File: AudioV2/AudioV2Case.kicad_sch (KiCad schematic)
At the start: 0 parts

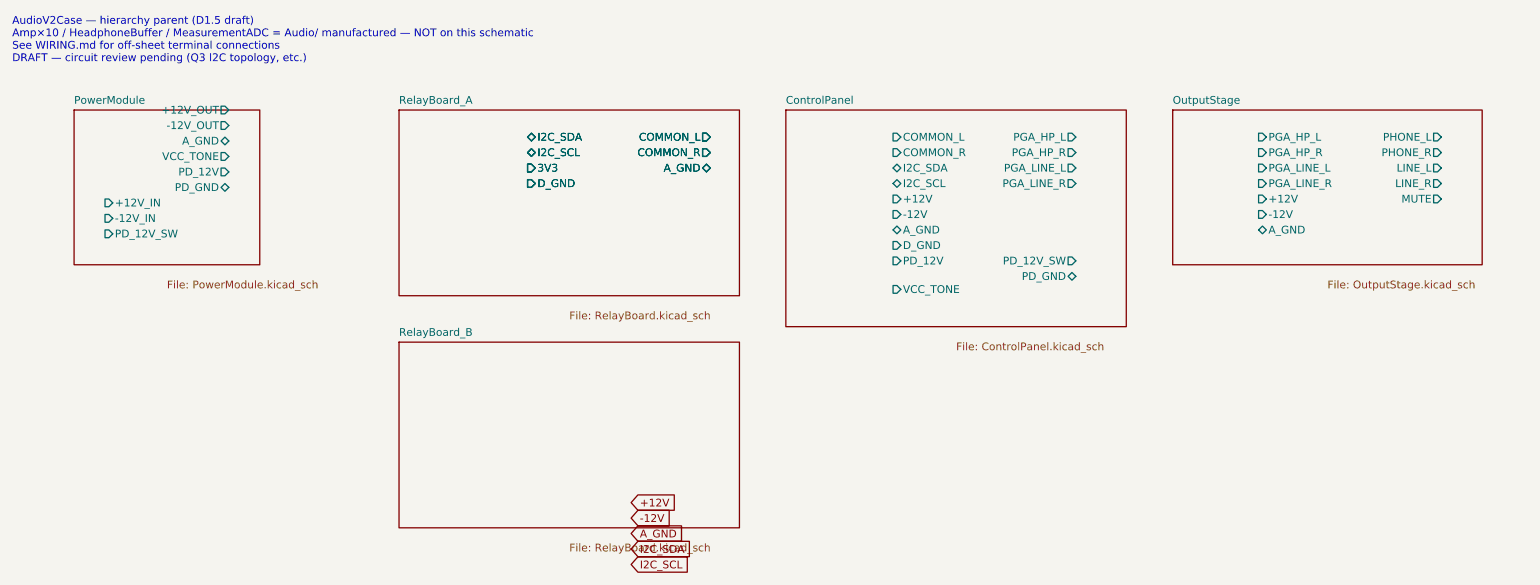
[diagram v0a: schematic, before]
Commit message: feat(AudioV2): CIRCUIT_DESIGNに沿って回路配置・配線（Control/Power/親）
- wire_circuit_design.py: PT2314 周辺 C/R、PGA2310 SPI/電源、7809、親バス
- PowerModule/ControlPanel/AudioV2Case を配線付きで再生成
- CIRCUIT_DESIGN.md チェックリスト更新

ERC は Relay/Output 未配線・親バス調整残り
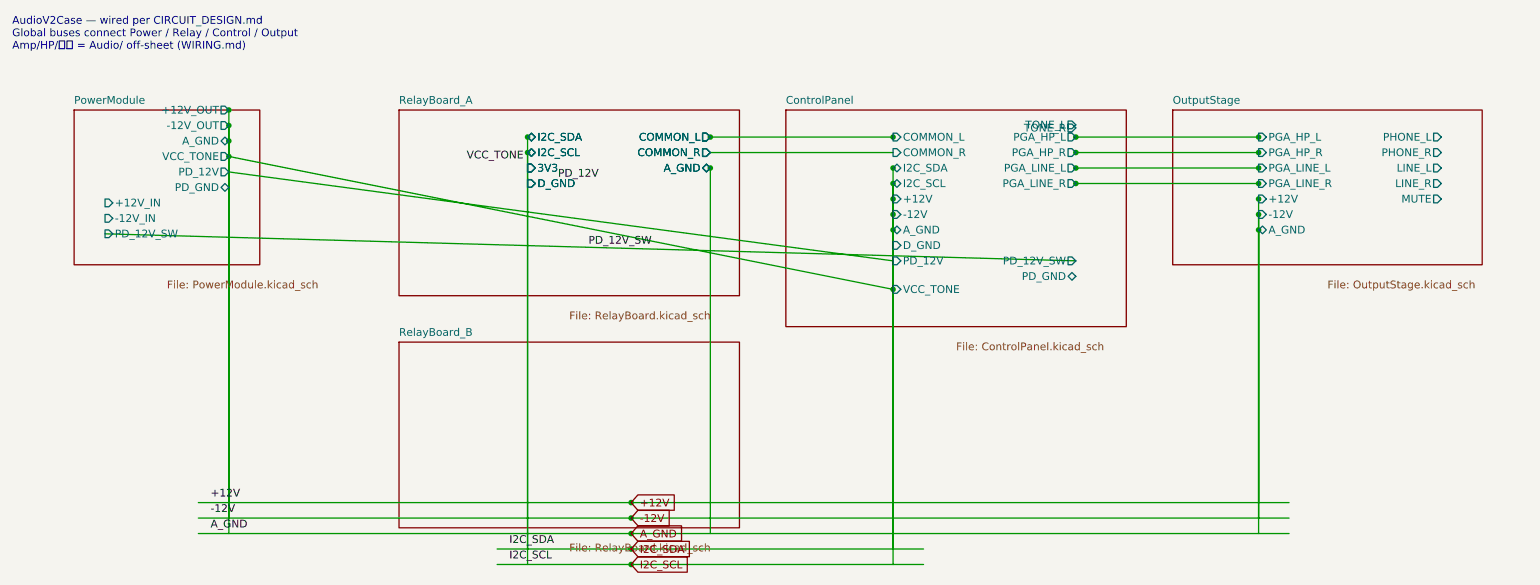
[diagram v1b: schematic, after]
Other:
- sheet ControlPanel ports: added TONE_L, TONE_R; removed none
- note added: "AudioV2Case — wired per CIRCUIT_DESIGN.md Global buses connect Power / Relay / Control / Output Amp/HP/計測 = Audio/ off-sheet (WIRING.md)"
- note removed: "AudioV2Case — hierarchy parent (D1.5 draft) Amp×10 / HeadphoneBuffer / MeasurementADC = Audio/ manufactured — NOT on this schematic See WIRING.md for off-sheet terminal connections DRAFT — circuit review pending (Q3 I2C topology, etc.)"
